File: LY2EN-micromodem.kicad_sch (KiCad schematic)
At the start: 19 parts

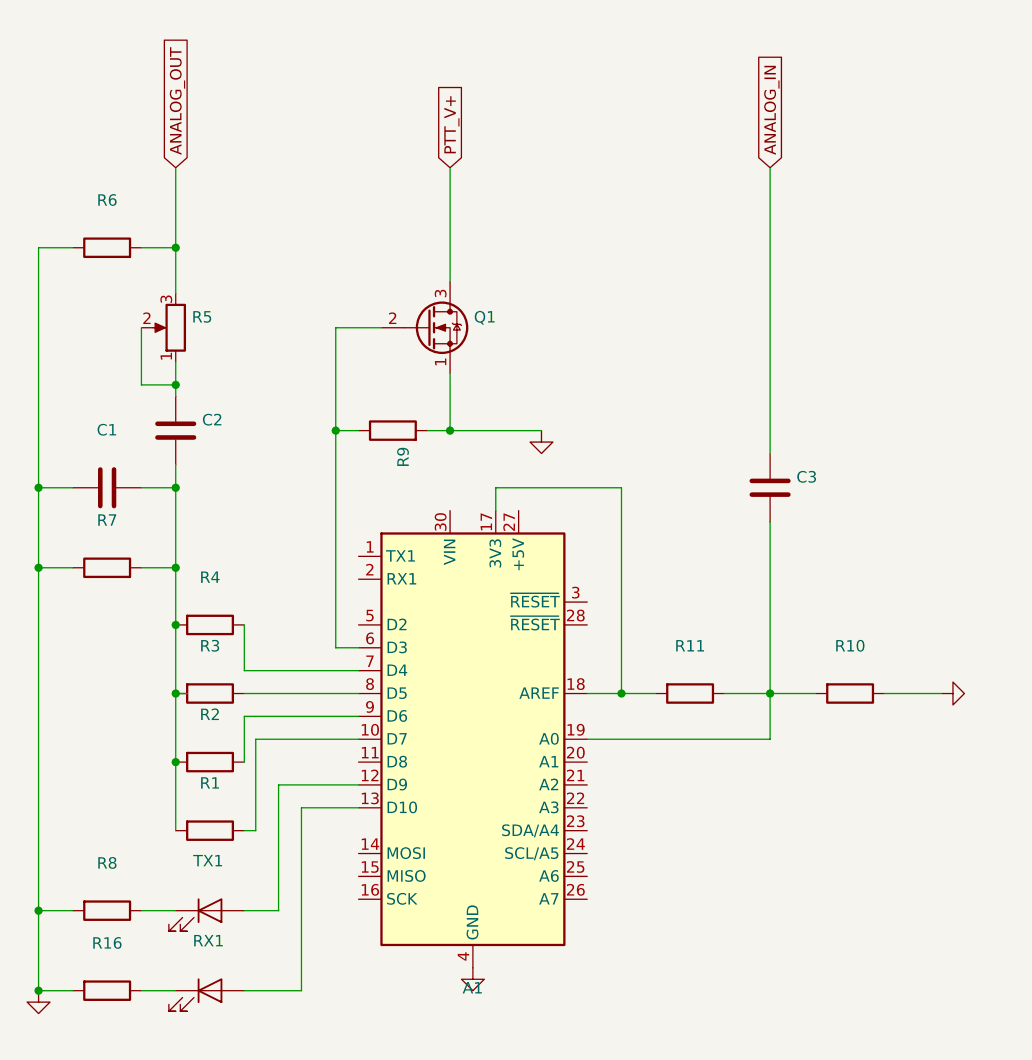
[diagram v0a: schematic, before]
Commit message: Add Bluetooth SPP-C serial passthrough support
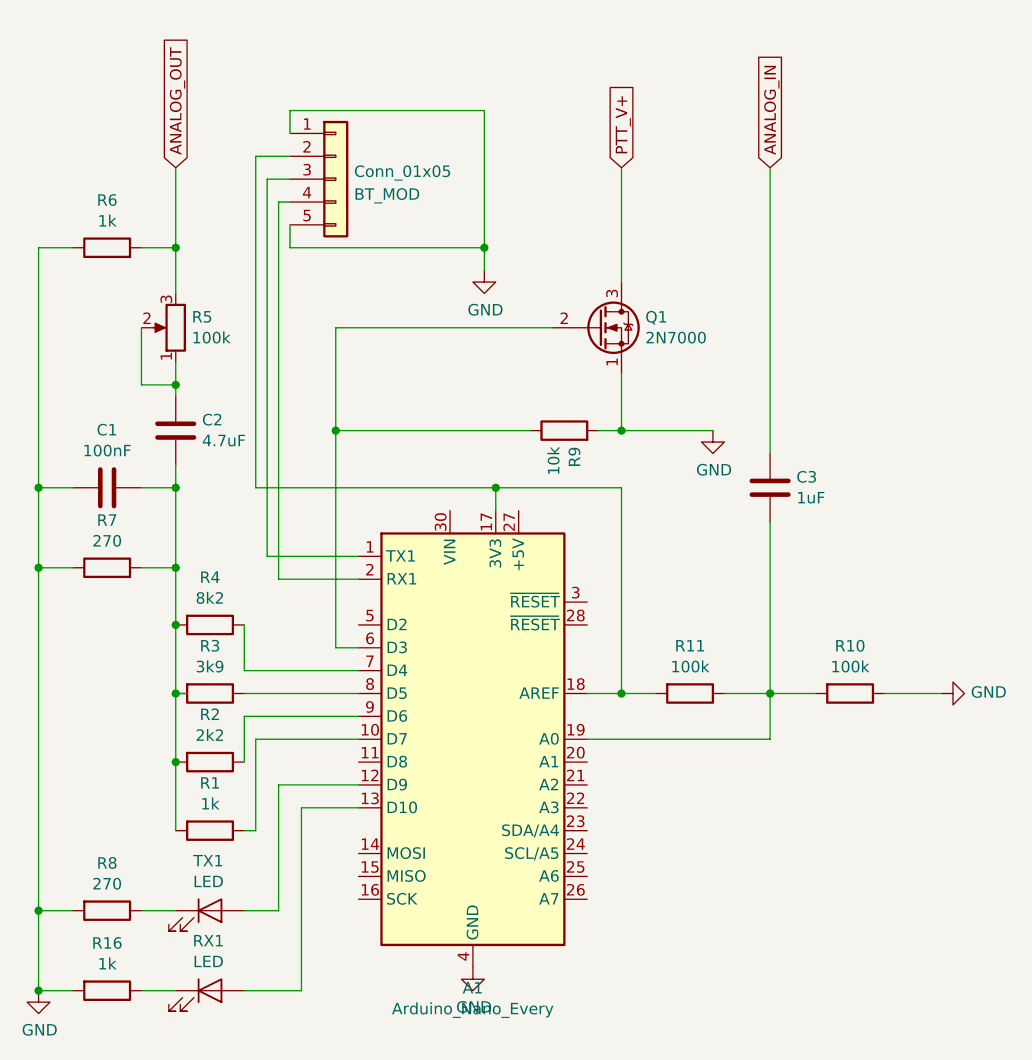
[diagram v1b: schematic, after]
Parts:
- added Conn_01x05: BT_MOD, Connector_PinSocket_2.54mm:PinSocket_1x05_P2.54mm_Vertical, symbol Connector_Generic:Conn_01x05
- A1: value (none) -> Arduino_Nano_Every; footprint (none) -> Module:Arduino_Nano_WithMountingHoles
- C1: value (none) -> 100nF; footprint (none) -> Capacitor_SMD:C_0805_2012Metric_Pad1.18x1.45mm_HandSolder
- C2: value (none) -> 4.7uF; footprint (none) -> Capacitor_SMD:C_0805_2012Metric_Pad1.18x1.45mm_HandSolder
- C3: value (none) -> 1uF; footprint (none) -> Capacitor_SMD:C_0805_2012Metric_Pad1.18x1.45mm_HandSolder
- Q1: value (none) -> 2N7000; footprint (none) -> Package_TO_SOT_THT:TO-92_Inline
- R1, R16, R6: value (none) -> 1k; footprint (none) -> Resistor_SMD:R_0805_2012Metric_Pad1.20x1.40mm_HandSolder
- R10, R11: value (none) -> 100k; footprint (none) -> Resistor_SMD:R_0805_2012Metric_Pad1.20x1.40mm_HandSolder
- R2: value (none) -> 2k2; footprint (none) -> Resistor_SMD:R_0805_2012Metric_Pad1.20x1.40mm_HandSolder
- R3: value (none) -> 3k9; footprint (none) -> Resistor_SMD:R_0805_2012Metric_Pad1.20x1.40mm_HandSolder
- R4: value (none) -> 8k2; footprint (none) -> Resistor_SMD:R_0805_2012Metric_Pad1.20x1.40mm_HandSolder
- R5: value (none) -> 100k; footprint (none) -> Potentiometer_THT:Potentiometer_Bourns_3296W_Vertical
- R7, R8: value (none) -> 270; footprint (none) -> Resistor_SMD:R_0805_2012Metric_Pad1.20x1.40mm_HandSolder
- R9: value (none) -> 10k; footprint (none) -> Resistor_SMD:R_0805_2012Metric_Pad1.20x1.40mm_HandSolder
- RX1, TX1: value (none) -> LED; footprint (none) -> LED_SMD:LED_0805_2012Metric_Pad1.15x1.40mm_HandSolder
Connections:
- net GND: now also Conn_01x05.1 (Pin_1), Conn_01x05.5 (Pin_5)
- net at A1.1 (TX1): now also Conn_01x05.3 (Pin_3)
- net at A1.17 (3V3), A1.18 (AREF), R11.2: now also Conn_01x05.2 (Pin_2)
- net at A1.2 (RX1): now also Conn_01x05.4 (Pin_4)
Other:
- moved on the sheet: Q1, R9

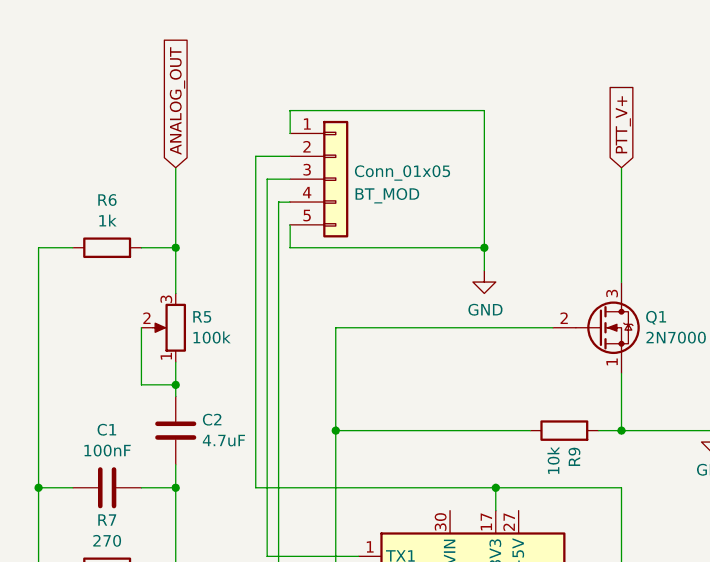
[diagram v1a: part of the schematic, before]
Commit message: Replace potentiometer with static 47k resistor
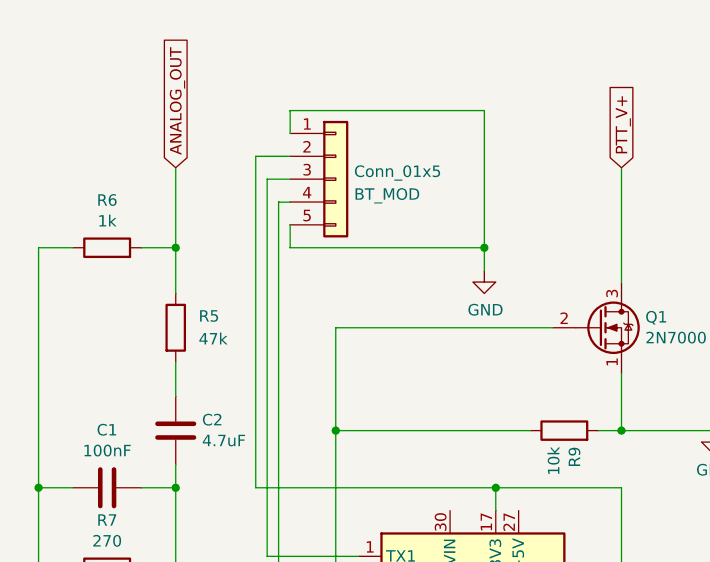
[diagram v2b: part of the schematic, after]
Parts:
- removed R5: 100k, Potentiometer_THT:Potentiometer_Bourns_3296W_Vertical, symbol Device:R_POT
- added R5: 47k, Resistor_SMD:R_0805_2012Metric_Pad1.20x1.40mm_HandSolder, symbol Device:R
- renumbered Conn_01x05 to Conn_01x5
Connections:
- net ANALOG_OUT: now also R5.1
- net at C2.1: now also R5.2
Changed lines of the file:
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@@
 (kicad_sch (version 20211123) (generator eeschema)
   (paper "A4")
-  (junction (at 124.46 67.31) (diameter 0) (color 0 0 0 0)
-  )
   (junction (at 109.22 87.63) (diameter 0) (color 0 0 0 0)
   )
@@
     (stroke (width 0) (type default) (color 0 0 0 0))
   )
-  (wire (pts (xy 124.46 67.31) (xy 124.46 68.58))
-    (stroke (width 0) (type default) (color 0 0 0 0))
-  )
   (wire (pts (xy 132.08 125.73) (xy 135.89 125.73))
     (stroke (width 0) (type default) (color 0 0 0 0))
@@
     (stroke (width 0) (type default) (color 0 0 0 0))
   )
-  (wire (pts (xy 124.46 64.77) (xy 124.46 67.31))
+  (wire (pts (xy 124.46 64.77) (xy 124.46 68.58))
     (stroke (width 0) (type default) (color 0 0 0 0))
   )
@@
     (stroke (width 0) (type default) (color 0 0 0 0))
   )
-  (wire (pts (xy 120.65 60.96) (xy 120.65 67.31))
-    (stroke (width 0) (type default) (color 0 0 0 0))
-  )
   (wire (pts (xy 125.73 101.6) (xy 124.46 101.6))
     (stroke (width 0) (type default) (color 0 0 0 0))
@@
   )
   (wire (pts (xy 133.35 78.74) (xy 160.02 78.74))
-    (stroke (width 0) (type default) (color 0 0 0 0))
-  )
-  (wire (pts (xy 120.65 67.31) (xy 124.46 67.31))
     (stroke (width 0) (type default) (color 0 0 0 0))
   )
@@
     (pin "9")
   )
-  (symbol (lib_id "Device:R_POT") (at 124.46 60.96 180) (unit 1)
-    (in_bom yes) (on_board yes)
-    (property "Reference" "R5" (id 0) (at 126.238 59.7916 0)
-      (effects (font (size 1.27 1.27)) (justify right))
-    )
-    (property "Value" "100k" (id 1) (at 126.238 62.103 0)
-      (effects (font (size 1.27 1.27)) (justify right))
-    )
-    (property "Footprint" "Potentiometer_THT:Potentiometer_Bourns_3296W_Vertical" (id 2) (at 124.46 60.96 0)
-      (effects (font (size 1.27 1.27)) hide)
-    )
-    (property "Datasheet" "~" (id 3) (at 124.46 60.96 0)
-      (effects (font (size 1.27 1.27)) hide)
-    )
-    (pin "1")
-    (pin "2")
-    (pin "3")
-  )
   (symbol (lib_id "power:GND") (at 109.22 134.62 0) (unit 1)
     (in_bom yes) (on_board yes)
@@
   (symbol (lib_id "Connector_Generic:Conn_01x05") (at 142.24 44.45 0) (unit 1)
     (in_bom yes) (on_board yes) (fields_autoplaced)
-    (property "Reference" "Conn_01x05" (id 0) (at 144.272 43.6153 0)
+    (property "Reference" "Conn_01x5" (id 0) (at 144.272 43.6153 0)
       (effects (font (size 1.27 1.27)) (justify left))
     )
@@
     (pin "5")
   )
+  (symbol (lib_id "Device:R") (at 124.46 60.96 0) (unit 1)
+    (in_bom yes) (on_board yes) (fields_autoplaced)
+    (property "Reference" "R5" (id 0) (at 127 59.6899 0)
+      (effects (font (size 1.27 1.27)) (justify left))
+    )
+    (property "Value" "47k" (id 1) (at 127 62.2299 0)
+      (effects (font (size 1.27 1.27)) (justify left))
+    )
+    (property "Footprint" "Resistor_SMD:R_0805_2012Metric_Pad1.20x1.40mm_HandSolder" (id 2) (at 122.682 60.96 90)
+      (effects (font (size 1.27 1.27)) hide)
+    )
+    (property "Datasheet" "~" (id 3) (at 124.46 60.96 0)
+      (effects (font (size 1.27 1.27)) hide)
+    )
+    (pin "1")
+    (pin "2")
+  )
   (symbol (lib_id "power:GND") (at 158.75 54.61 0) (unit 1)
     (in_bom yes) (on_board yes)
@@
     )
     (path "/474dbcf6-c00b-4ec7-aaf4-470095c0dd4c"
-      (reference "Conn_01x05") (unit 1) (value "BT_MOD") (footprint "Connector_PinSocket_2.54mm:PinSocket_1x05_P2.54mm_Vertical")
+      (reference "Conn_01x5") (unit 1) (value "BT_MOD") (footprint "Connector_PinSocket_2.54mm:PinSocket_1x05_P2.54mm_Vertical")
     )
     (path "/00000000-0000-0000-0000-00006087291f"
@@
       (reference "R4") (unit 1) (value "8k2") (footprint "Resistor_SMD:R_0805_2012Metric_Pad1.20x1.40mm_HandSolder")
     )
-    (path "/00000000-0000-0000-0000-0000608605c0"
-      (reference "R5") (unit 1) (value "100k") (footprint "Potentiometer_THT:Potentiometer_Bourns_3296W_Vertical")
+    (path "/6e14ca46-4388-471b-929f-15c839f14dbe"
+      (reference "R5") (unit 1) (value "47k") (footprint "Resistor_SMD:R_0805_2012Metric_Pad1.20x1.40mm_HandSolder")
     )
     (path "/00000000-0000-0000-0000-00006087d77a"
